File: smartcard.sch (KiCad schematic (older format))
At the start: 49 parts, among them J1001 FILTER, J1706 TARGET_TRIG, P1000 ISO7816_NO, Q5001 BSS84, Q5002 BSS84, U1100 FOD8001, U1200 FOD8001, U1300 FOD8001, U1400 FOD8001, U1500 FOD8001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

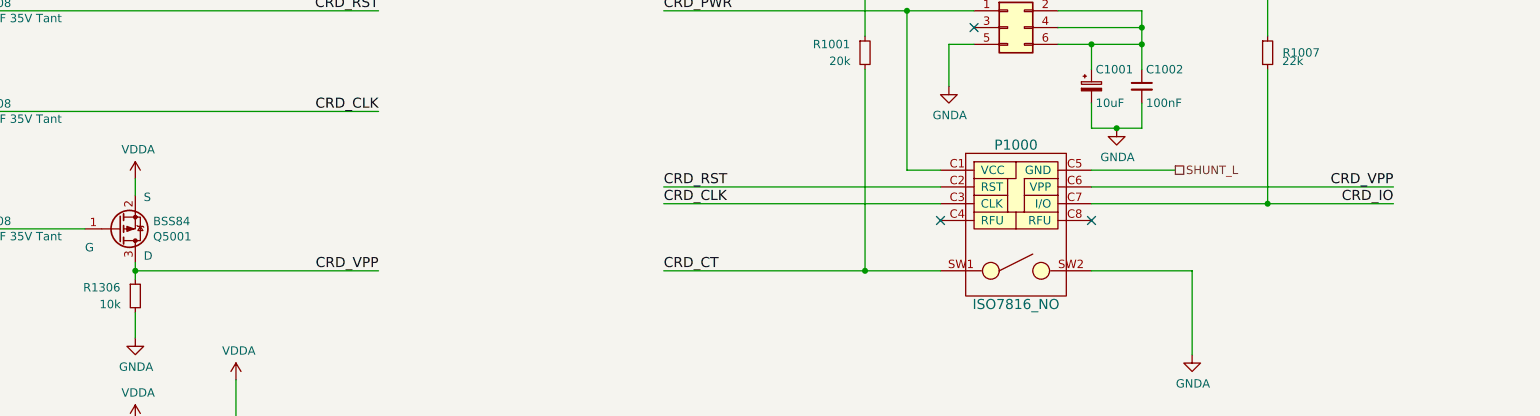
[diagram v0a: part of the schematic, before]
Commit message: [enhancement] Add tests points for smartcard controlled triggers, connect PB4 to CARD_CLK for bitbanging mode
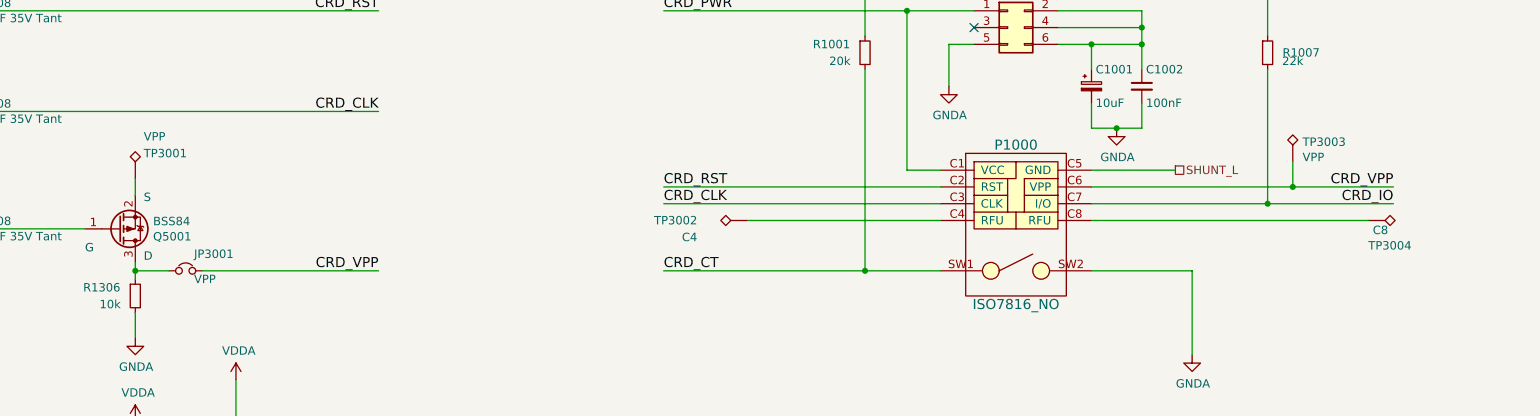
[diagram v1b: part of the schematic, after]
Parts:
- added JP3001: VPP, Connector_PinHeader_2.54mm:PinHeader_1x02_P2.54mm_Vertical, symbol Device:Jumper_NC_Small
- added TP3001, TP3003: VPP, TestPoint_Keystone_5000-5004_Miniature, symbol Connector:TestPoint_Alt
- added TP3002: C4, TestPoint_Keystone_5000-5004_Miniature, symbol Connector:TestPoint_Alt
- added TP3004: C8, TestPoint_Keystone_5000-5004_Miniature, symbol Connector:TestPoint_Alt
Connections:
- net CRD_VPP: now also JP3001.2, TP3003.1; no longer Q5001.3 (D), R1306.1
- net VDDA: no longer Q5001.2 (S)
- net at P1000.C4 (RFU): now also TP3002.1
- net at P1000.C8 (RFU): now also TP3004.1
- new net: JP3001.1, Q5001.3 (D), R1306.1
- new net: Q5001.2 (S), TP3001.1
- no-connect marks 3 -> 1
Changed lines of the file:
@@
 Text Label 9150 8650 2    60   ~ 0
 CRD_PWR
-NoConn ~ 12450 4900
-NoConn ~ 13350 4900
 Wire Wire Line
 	13950 5200 13950 5700
@@
 Wire Wire Line
 	10800 4700 12450 4700
-Wire Wire Line
-	13350 4700 15150 4700
 $Comp
 L Connector:Conn_Coaxial J1706
@@
 	3650 6850 4650 6850
 $Comp
-L power:VDDA #PWR0118
-U 1 1 5CAA88D4
-P 7650 4650
-F 0 "#PWR0118" H 7650 4500 50  0001 C CNN
-F 1 "VDDA" H 7667 4823 50  0000 C CNN
-F 2 "" H 7650 4650 50  0001 C CNN
-F 3 "" H 7650 4650 50  0001 C CNN
-	1    7650 4650
-	1    0    0    -1
-$EndComp
-$Comp
 L Device:R_Small R1306
 U 1 1 5CAD467F
@@
 	7650 5450 7650 5600
 Wire Wire Line
-	7650 5200 9100 5200
+	7650 5200 7850 5200
 Wire Wire Line
 	7650 5150 7650 5200
@@
 Text Notes 8000 8200 0    50   ~ 0
 S
+Wire Wire Line
+	13350 4700 14550 4700
+$Comp
+L Connector:TestPoint_Alt TP3003
+U 1 1 5D081D31
+P 14550 4550
+AR Path="/5B19B7B2/5D081D31" Ref="TP3003"  Part="1"
+AR Path="/5CD07BF2/5D081D31" Ref="TP?"  Part="1"
+AR Path="/5D081D31" Ref="TP?"  Part="1"
+AR Path="/5CBC3017/5D081D31" Ref="TP?"  Part="1"
+F 0 "TP3003" H 14608 4668 50  0000 L CNN
+F 1 "VPP" H 14608 4577 50  0000 L CNN
+F 2 "TestPoint_Keystone_5000-5004_Miniature" H 14750 4550 50  0001 C CNN
+F 3 "~" H 14750 4550 50  0001 C CNN
+F 4 "KEYSTONE" H 10550 7250 50  0001 C CNN "MFG Name"
+F 5 "5001" H 10550 7250 50  0001 C CNN "MFG Part Num"
+F 6 "Farnell" H 10550 7250 50  0001 C CNN "Distrib Name"
+F 7 "Farnell" H 4750 100 50  0001 C CNN "Distrib"
+F 8 "http://fr.farnell.com/c-k-components/ksr231g-lfs/tactile-commutateur-miniature/dp/1201422" H 4750 100 50  0001 C CNN "Distrib Link"
+F 9 "2301278" H 4750 100 50  0001 C CNN "Distrib PN"
+F 10 "5001" H 4750 100 50  0001 C CNN "Mouser Price/Stock"
+	1    14550 4550
+	1    0    0    -1
+$EndComp
+Wire Wire Line
+	14550 4550 14550 4700
+Connection ~ 14550 4700
+Wire Wire Line
+	14550 4700 15150 4700
+$Comp
+L Connector:TestPoint_Alt TP3002
+U 1 1 5D0C6C9F
+P 11300 4900
+AR Path="/5B19B7B2/5D0C6C9F" Ref="TP3002"  Part="1"
+AR Path="/5CD07BF2/5D0C6C9F" Ref="TP?"  Part="1"
+AR Path="/5D0C6C9F" Ref="TP?"  Part="1"
+AR Path="/5CBC3017/5D0C6C9F" Ref="TP?"  Part="1"
+F 0 "TP3002" V 11300 5200 50  0000 L CNN
+F 1 "C4" V 11200 5200 50  0000 L CNN
+F 2 "TestPoint_Keystone_5000-5004_Miniature" H 11500 4900 50  0001 C CNN
+F 3 "~" H 11500 4900 50  0001 C CNN
+F 4 "KEYSTONE" H 7300 7600 50  0001 C CNN "MFG Name"
+F 5 "5001" H 7300 7600 50  0001 C CNN "MFG Part Num"
+F 6 "Farnell" H 7300 7600 50  0001 C CNN "Distrib Name"
+F 7 "Farnell" H 1500 450 50  0001 C CNN "Distrib"
+F 8 "http://fr.farnell.com/c-k-components/ksr231g-lfs/tactile-commutateur-miniature/dp/1201422" H 1500 450 50  0001 C CNN "Distrib Link"
+F 9 "2301278" H 1500 450 50  0001 C CNN "Distrib PN"
+F 10 "5001" H 1500 450 50  0001 C CNN "Mouser Price/Stock"
+	1    11300 4900
+	0    -1   -1   0
+$EndComp
+$Comp
+L Connector:TestPoint_Alt TP3004
+U 1 1 5D0C7BBC
+P 15000 4900
+AR Path="/5B19B7B2/5D0C7BBC" Ref="TP3004"  Part="1"
+AR Path="/5CD07BF2/5D0C7BBC" Ref="TP?"  Part="1"
+AR Path="/5D0C7BBC" Ref="TP?"  Part="1"
+AR Path="/5CBC3017/5D0C7BBC" Ref="TP?"  Part="1"
+F 0 "TP3004" V 15150 4900 50  0000 L CNN
+F 1 "C8" V 15058 4927 50  0000 L CNN
+F 2 "TestPoint_Keystone_5000-5004_Miniature" H 15200 4900 50  0001 C CNN
+F 3 "~" H 15200 4900 50  0001 C CNN
+F 4 "KEYSTONE" H 11000 7600 50  0001 C CNN "MFG Name"
+F 5 "5001" H 11000 7600 50  0001 C CNN "MFG Part Num"
+F 6 "Farnell" H 11000 7600 50  0001 C CNN "Distrib Name"
+F 7 "Farnell" H 5200 450 50  0001 C CNN "Distrib"
+F 8 "http://fr.farnell.com/c-k-components/ksr231g-lfs/tactile-commutateur-miniature/dp/1201422" H 5200 450 50  0001 C CNN "Distrib Link"
+F 9 "2301278" H 5200 450 50  0001 C CNN "Distrib PN"
+F 10 "5001" H 5200 450 50  0001 C CNN "Mouser Price/Stock"
+	1    15000 4900
+	0    1    1    0
+$EndComp
+Wire Wire Line
+	11300 4900 12450 4900
+Wire Wire Line
+	13350 4900 15000 4900
+$Comp
+L Connector:TestPoint_Alt TP3001
+U 1 1 5CFCA9D3
+P 7650 4650
+AR Path="/5B19B7B2/5CFCA9D3" Ref="TP3001"  Part="1"
+AR Path="/5CD07BF2/5CFCA9D3" Ref="TP?"  Part="1"
+AR Path="/5CFCA9D3" Ref="TP?"  Part="1"
+AR Path="/5CBC3017/5CFCA9D3" Ref="TP?"  Part="1"
+F 0 "TP3001" H 7700 4800 50  0000 L CNN
+F 1 "VPP" H 7700 4900 50  0000 L CNN
+F 2 "TestPoint_Keystone_5000-5004_Miniature" H 7850 4650 50  0001 C CNN
+F 3 "~" H 7850 4650 50  0001 C CNN
+F 4 "KEYSTONE" H 3650 7350 50  0001 C CNN "MFG Name"
+F 5 "5001" H 3650 7350 50  0001 C CNN "MFG Part Num"
+F 6 "Farnell" H 3650 7350 50  0001 C CNN "Distrib Name"
+F 7 "Farnell" H -2150 200 50  0001 C CNN "Distrib"
+F 8 "http://fr.farnell.com/c-k-components/ksr231g-lfs/tactile-commutateur-miniature/dp/1201422" H -2150 200 50  0001 C CNN "Distrib Link"
+F 9 "2301278" H -2150 200 50  0001 C CNN "Distrib PN"
+F 10 "5001" H -2150 200 50  0001 C CNN "Mouser Price/Stock"
+	1    7650 4650
+	1    0    0    -1
+$EndComp
+$Comp
+L Device:Jumper_NC_Small JP?
+U 1 1 5CFDED16
+P 7950 5200
+AR Path="/5B22B7CD/5CFDED16" Ref="JP?"  Part="1"
+AR Path="/5B19B7B2/5CFDED16" Ref="JP3001"  Part="1"
+AR Path="/5CBC3017/5B19B7B2/5CFDED16" Ref="JP?"  Part="1"
+F 0 "JP3001" H 8000 5300 50  0000 L CNN
+F 1 "VPP" H 8000 5150 50  0000 L CNN
+F 2 "Connector_PinHeader_2.54mm:PinHeader_1x02_P2.54mm_Vertical" H 7950 5200 50  0001 C CNN
+F 3 "~" H 7950 5200 50  0001 C CNN
+F 4 "Molex" V 7950 5200 50  0001 C CNN "MFG Name"
+F 5 "90120-0762" V 7950 5200 50  0001 C CNN "MFG Part Num"
+F 6 "2751456" V 7950 5200 50  0001 C CNN "Distrib PN"
+F 7 "Farnell" V 7950 5200 50  0001 C CNN "Distrib"
+F 8 "Farnell" H 1350 -2700 50  0001 C CNN "Distrib Name"
+	1    7950 5200
+	1    0    0    -1
+$EndComp
+Wire Wire Line
+	8050 5200 9100 5200
 $EndSCHEMATC
